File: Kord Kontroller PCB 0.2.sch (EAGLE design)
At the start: 191 parts, among them IC2 74HCT1G125DBV, J1 MIDIOUTB, J2 MIDIOUTA, J3 FTSH-105-01-L-DV-KJ, SW2 SPST_TACT-KMR2, U1 AP2112K-3.3, U2 ATSAMD51J19A-AUT, X3 microUSB

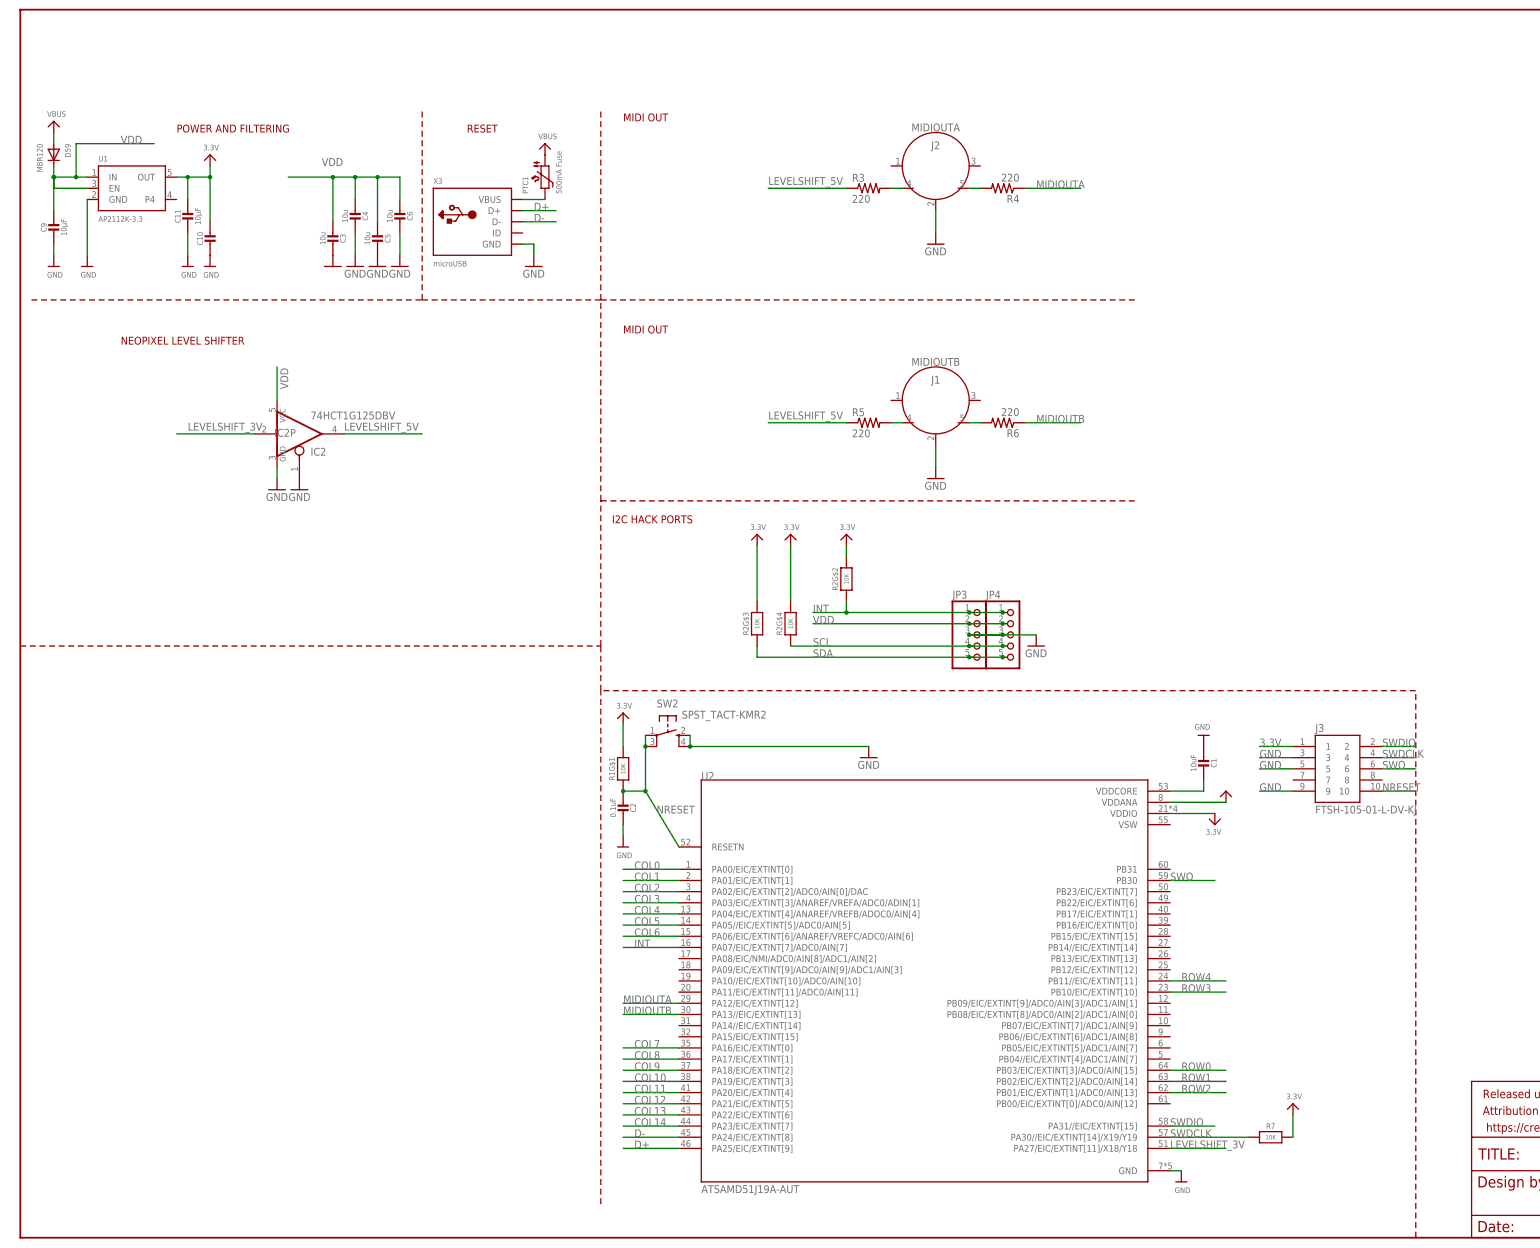
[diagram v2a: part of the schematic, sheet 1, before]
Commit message: traced routes for LEDs and half the board
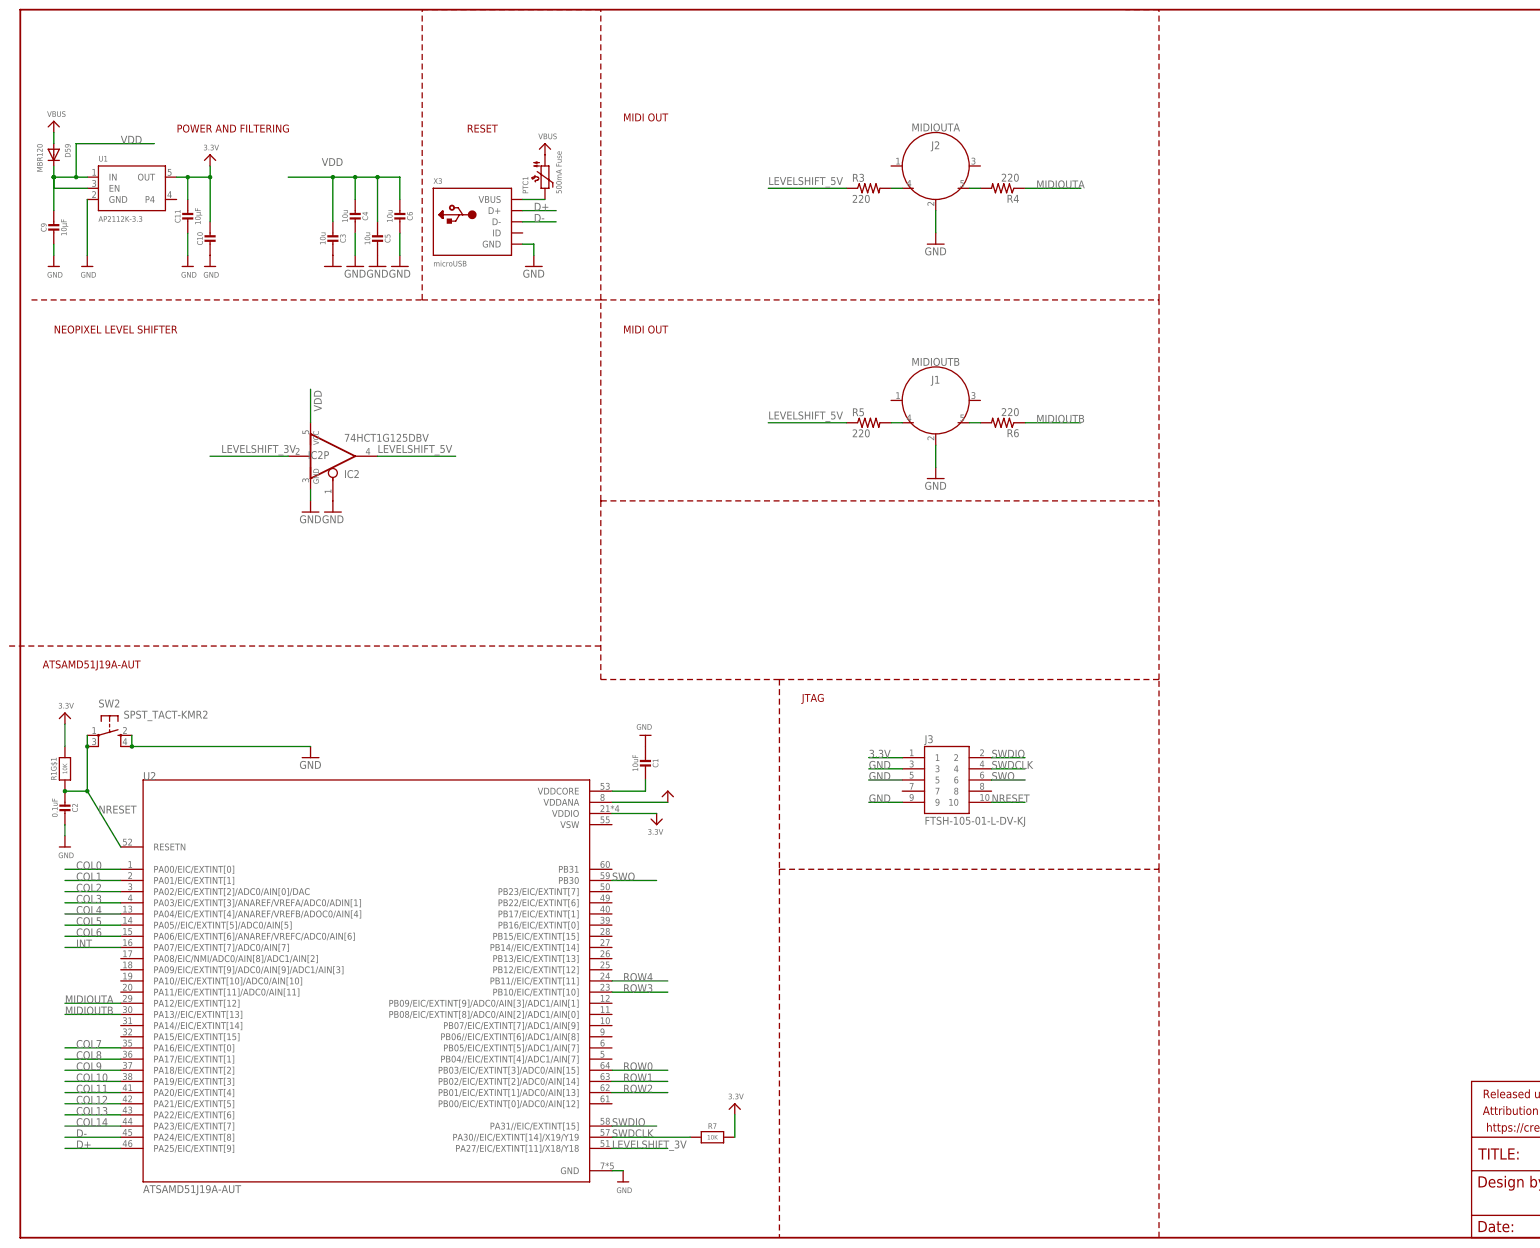
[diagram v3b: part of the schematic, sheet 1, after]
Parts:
- removed JP3, JP4: (no value), microbuilder:HEADER-1X5EDGESMT
- removed R2: 10K, microbuilder:RESISTOR_4PACK
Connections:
- removed net N$104: LED50.DO, LED52.DI
- removed net N$105: LED51.DI, LED52.DO
- removed net N$106: LED51.DO, LED53.DI
- removed net N$90: LED34.DO, LED36.DI
- removed net N$91: LED35.DI, LED36.DO
- removed net N$92: LED35.DO, LED37.DI
- removed net N$97: LED42.DO, LED44.DI
- removed net N$98: LED43.DI, LED44.DO
- removed net N$99: LED43.DO, LED45.DI
- removed net SCL: JP3.4, JP4.4, R2G$4.1
- removed net SDA: JP3.5, JP4.5, R2G$3.1
- new net N$3: LED36.DO, LED37.DI
- new net N$49: LED34.DO, LED35.DI
- new net N$50: LED35.DO, LED36.DI
- new net N$51: LED44.DO, LED45.DI
- new net N$55: LED43.DO, LED44.DI
- new net N$59: LED42.DO, LED43.DI
- new net N$65: LED50.DO, LED51.DI
- new net N$67: LED51.DO, LED52.DI
- new net N$68: LED52.DO, LED53.DI
- net 3.3V: no longer R2G$2.2, R2G$3.2, R2G$4.2
- net GND: no longer JP3.3, JP4.3
- net INT: no longer JP3.1, JP4.1, R2G$2.1
- net N$30: now also LED11.DI; no longer LED12.DI
- net N$31: now also LED11.DO, LED12.DI; no longer LED11.DI, LED12.DO
- net N$32: now also LED12.DO; no longer LED11.DO
- net N$42: now also LED27.DI; no longer LED28.DI
- net N$43: now also LED29.DI; no longer LED27.DI
- net N$44: now also LED28.DI; no longer LED29.DI
- net VDD: no longer JP3.2, JP4.2
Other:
- note added: "ATSAMD51J19A-AUT"
- note added: "JTAG"
- note removed: "I2C HACK PORTS"
- moved on the sheet: C1, C2, IC2, IC2P, J3, R1G$1, R7, SW2, U2
